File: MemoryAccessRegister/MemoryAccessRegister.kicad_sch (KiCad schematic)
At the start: 16 parts, among them J1 Conn_01x04_Pin, J2 Conn_01x04_Pin, J3 Conn_01x06_Pin, SW1 SW_SPDT, U1 CD74HCT258E, U3 74LS173

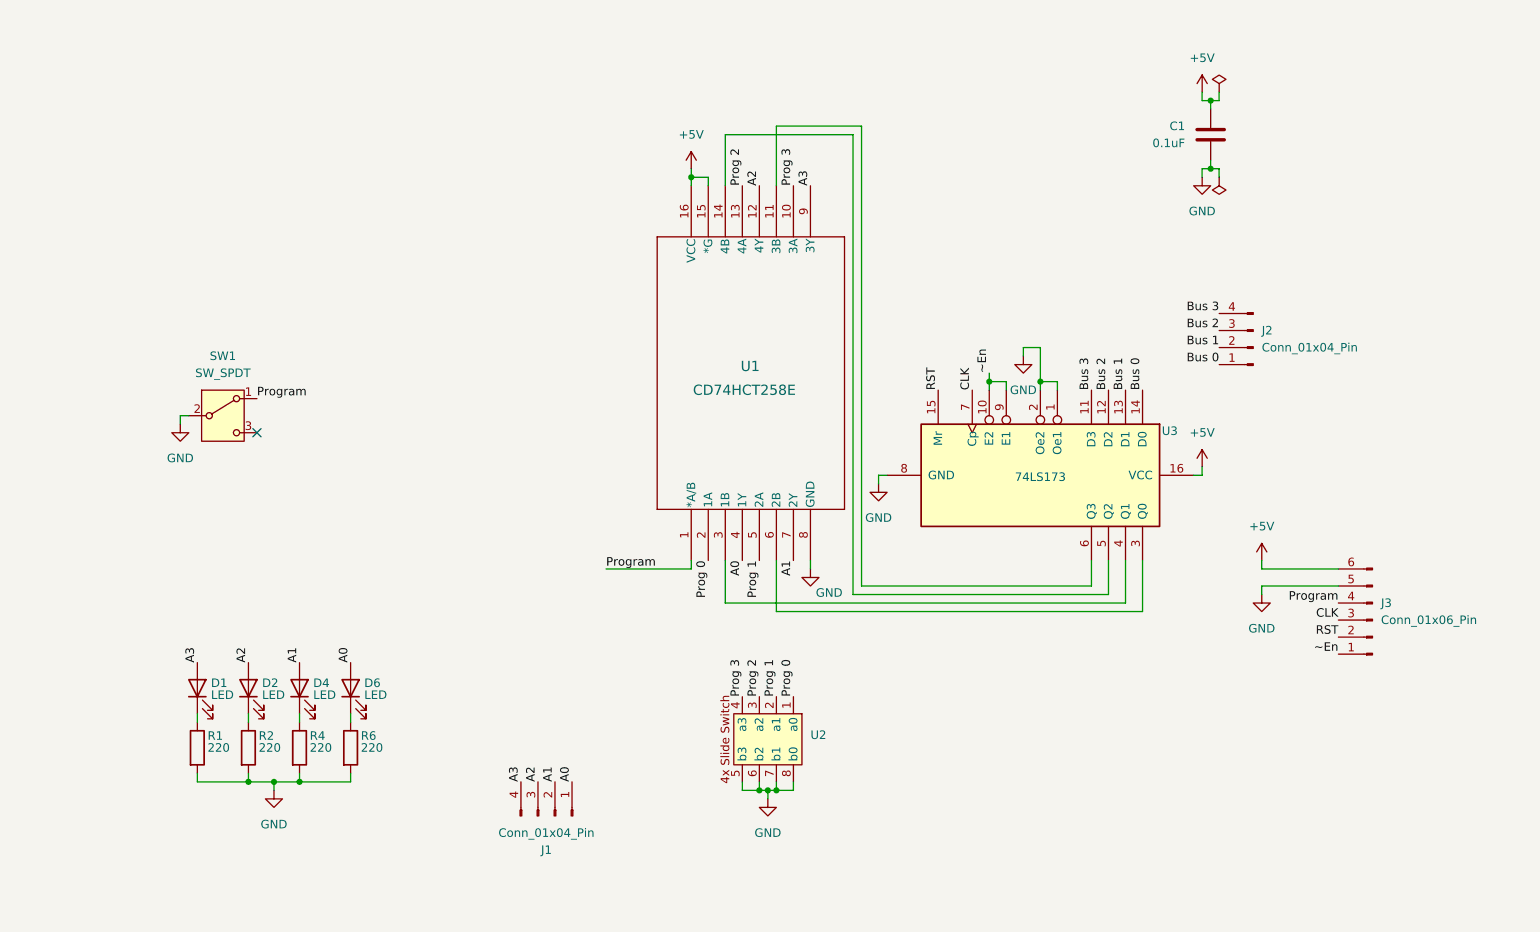
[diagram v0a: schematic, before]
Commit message: Fixed LED and pin footprints for MAR and cleaned up the layout
Fixed LED and pin footprints for MAR and cleaned up the layout
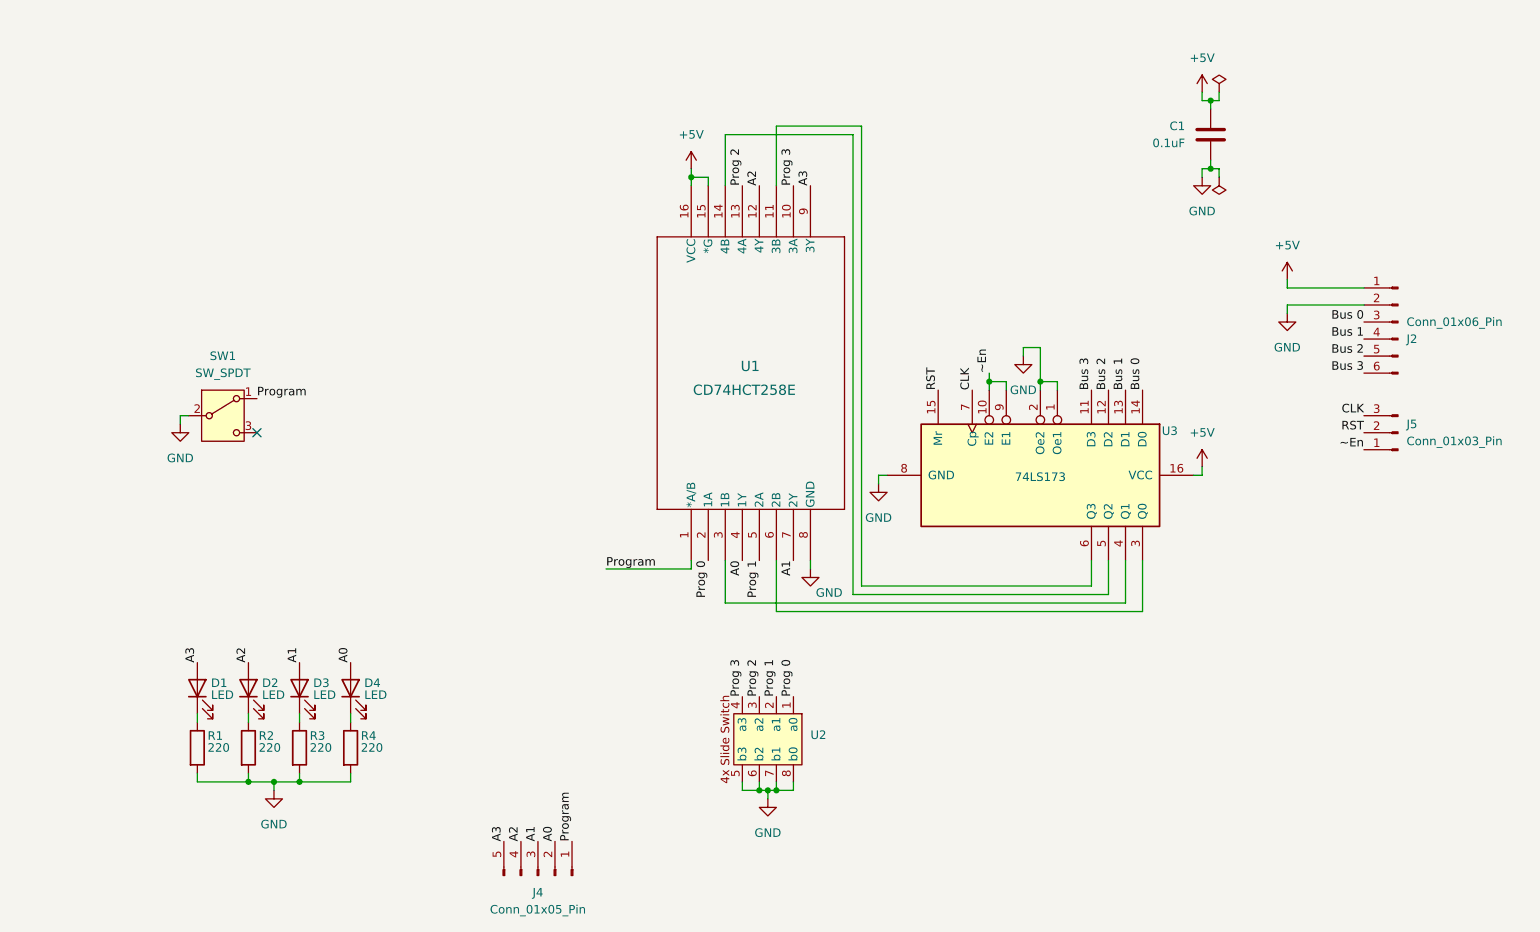
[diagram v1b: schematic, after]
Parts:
- removed J1, J2: Conn_01x04_Pin, Connector_PinHeader_1.00mm:PinHeader_1x04_P1.00mm_Horizontal, symbol Connector:Conn_01x04_Pin
- added J4: Conn_01x05_Pin, Connector_PinHeader_2.54mm:PinHeader_1x05_P2.54mm_Vertical, symbol Connector:Conn_01x05_Pin
- added J5: Conn_01x03_Pin, Connector_PinHeader_2.54mm:PinHeader_1x03_P2.54mm_Vertical, symbol Connector:Conn_01x03_Pin
- D1, D2: footprint LED_THT:LED_D2.0mm_W4.8mm_H2.5mm_FlatTop -> LED_THT:LED_D5.0mm
- D3: renamed from D4; footprint LED_THT:LED_D2.0mm_W4.8mm_H2.5mm_FlatTop -> LED_THT:LED_D5.0mm
- D4: renamed from D6; footprint LED_THT:LED_D2.0mm_W4.8mm_H2.5mm_FlatTop -> LED_THT:LED_D5.0mm
- J2: renamed from J3; footprint Connector_PinHeader_1.00mm:PinHeader_1x06_P1.00mm_Horizontal -> Connector_PinHeader_2.54mm:PinHeader_1x06_P2.54mm_Vertical
- renumbered R4 to R3, R6 to R4
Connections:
- net +5V: now also J2.1 (Pin_1); no longer J2.6 (Pin_6)
- net A0: now also J4.2 (Pin_2)
- net A1: now also J4.3 (Pin_3)
- net A2: now also J4.4 (Pin_4)
- net A3: now also J4.5 (Pin_5)
- net Bus 0: now also J2.3 (Pin_3)
- net Bus 1: now also J2.4 (Pin_4)
- net Bus 2: now also J2.5 (Pin_5)
- net Bus 3: now also J2.6 (Pin_6)
- net CLK: now also J5.3 (Pin_3); no longer J2.3 (Pin_3)
- net GND: now also J2.2 (Pin_2); no longer J2.5 (Pin_5)
- net Program: now also J4.1 (Pin_1); no longer J2.4 (Pin_4)
- net RST: now also J5.2 (Pin_2); no longer J2.2 (Pin_2)
- net ~En: now also J5.1 (Pin_1); no longer J2.1 (Pin_1)
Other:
- moved on the sheet: J2

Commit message: Fixed misrouted bus connections to MUX. MUX is inverting so adde inverterto invert back. Slide switch should be conencted to power and pulled to ground. Breadboard validated.
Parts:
- added R5, R6, R7, R8, R9: 1k, _DownloadFootprints:CF_series_Resistors_THT, symbol Device:R
- added U1: SN74AC14N, _DownloadFootprints:6x_not, symbol 6x_not:SN74AC14N
- renumbered J4 to J1, J5 to J3, U1 to U2, U2 to U3, U3 to U4
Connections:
- net +5V: now also U3.1 (a0), U3.2 (a1), U3.3 (a2), U3.4 (a3), R5.1, U1.14 (VCC); no longer U2.15 (*G)
- net A0: now also U1.2 (1Y); no longer U2.4 (1Y)
- net A1: now also U1.4 (2Y); no longer U2.7 (2Y)
- net A2: now also U1.6 (3Y); no longer U2.12 (4Y)
- net A3: now also U1.8 (4Y); no longer U2.9 (3Y)
- net GND: now also U2.15 (*G), R6.2, R7.2, R8.2, R9.2, U1.7 (GND); no longer U3.5 (b3), U3.6 (b2), U3.7 (b1), U3.8 (b0)
- net Prog 0: now also U3.5 (b3), R9.1; no longer U3.1 (a0)
- net Prog 1: now also U3.6 (b2), R8.1; no longer U3.2 (a1)
- net Prog 2: now also U3.7 (b1), R7.1; no longer U3.3 (a2)
- net Prog 3: now also U3.8 (b0), R6.1; no longer U3.4 (a3)
- net Program: now also R5.2
- net B3: now reaches U2.11 (3B), U4.6 (Q3)
- net B2: now reaches U2.14 (4B), U4.5 (Q2)
- net B0: now reaches U2.3 (1B)
- net B0: now also U4.3 (Q0); no longer U4.4 (Q1)
- net B1: now reaches U2.6 (2B)
- net B1: now also U4.4 (Q1); no longer U4.3 (Q0)
- new net ~A0: U1.1 (1A), U2.4 (1Y)
- new net ~A1: U1.3 (2A), U2.7 (2Y)
- new net ~A2: U1.5 (3A), U2.12 (4Y)
- new net ~A3: U1.9 (4A), U2.9 (3Y)
- no-connect marks 1 -> 5
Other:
- moved on the sheet: U3

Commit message: MAR layout complete
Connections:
- net A0: now also U1.6 (3Y); no longer U1.2 (1Y)
- net A2: now also U1.2 (1Y); no longer U1.6 (3Y)
- net ~A0: now also U1.5 (3A); no longer U1.1 (1A)
- net ~A2: now also U1.1 (1A); no longer U1.5 (3A)
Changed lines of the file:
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@@
 	)
 	(label "~A2"
-		(at 66.04 36.83 180)
+		(at 66.04 26.67 180)
 		(fields_autoplaced yes)
 		(effects
@@
 	)
 	(label "A2"
-		(at 66.04 39.37 180)
+		(at 66.04 29.21 180)
 		(fields_autoplaced yes)
 		(effects
@@
 	)
 	(label "~A0"
-		(at 66.04 26.67 180)
+		(at 66.04 36.83 180)
 		(fields_autoplaced yes)
 		(effects
@@
 	)
 	(label "A0"
-		(at 66.04 29.21 180)
-		(fields_autoplaced yes)
-		(effects
+		(at 66.04 39.37 180)
+		(fields_autoplaced yes)
+		(effects

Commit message: Manufacturer footprint and data sheet seem to be wrong for the mux. Input for bits 3 and 4 are swapped.
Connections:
- net B2: now also U2.13 (4B); no longer U2.14 (4B)
- net B3: now also U2.10 (3B); no longer U2.11 (3B)
- net Prog 2: now also U2.14 (4A); no longer U2.13 (4A)
- net Prog 3: now also U2.11 (3A); no longer U2.10 (3A)
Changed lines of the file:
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@@
 	)
 	(label "Prog 3"
-		(at 177.8 40.64 90)
+		(at 175.26 40.64 90)
 		(fields_autoplaced yes)
 		(effects
@@
 	)
 	(label "Prog 2"
-		(at 170.18 40.64 90)
+		(at 167.64 40.64 90)
 		(fields_autoplaced yes)
 		(effects
@@
 	)
 	(label "B2"
-		(at 167.64 40.64 90)
+		(at 170.18 40.64 90)
 		(fields_autoplaced yes)
 		(effects
@@
 	)
 	(label "B3"
-		(at 175.26 40.64 90)
-		(fields_autoplaced yes)
-		(effects
+		(at 177.8 40.64 90)
+		(fields_autoplaced yes)
+		(effects
